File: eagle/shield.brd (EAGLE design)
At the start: 63.2 x 55.9 mm, 12 parts

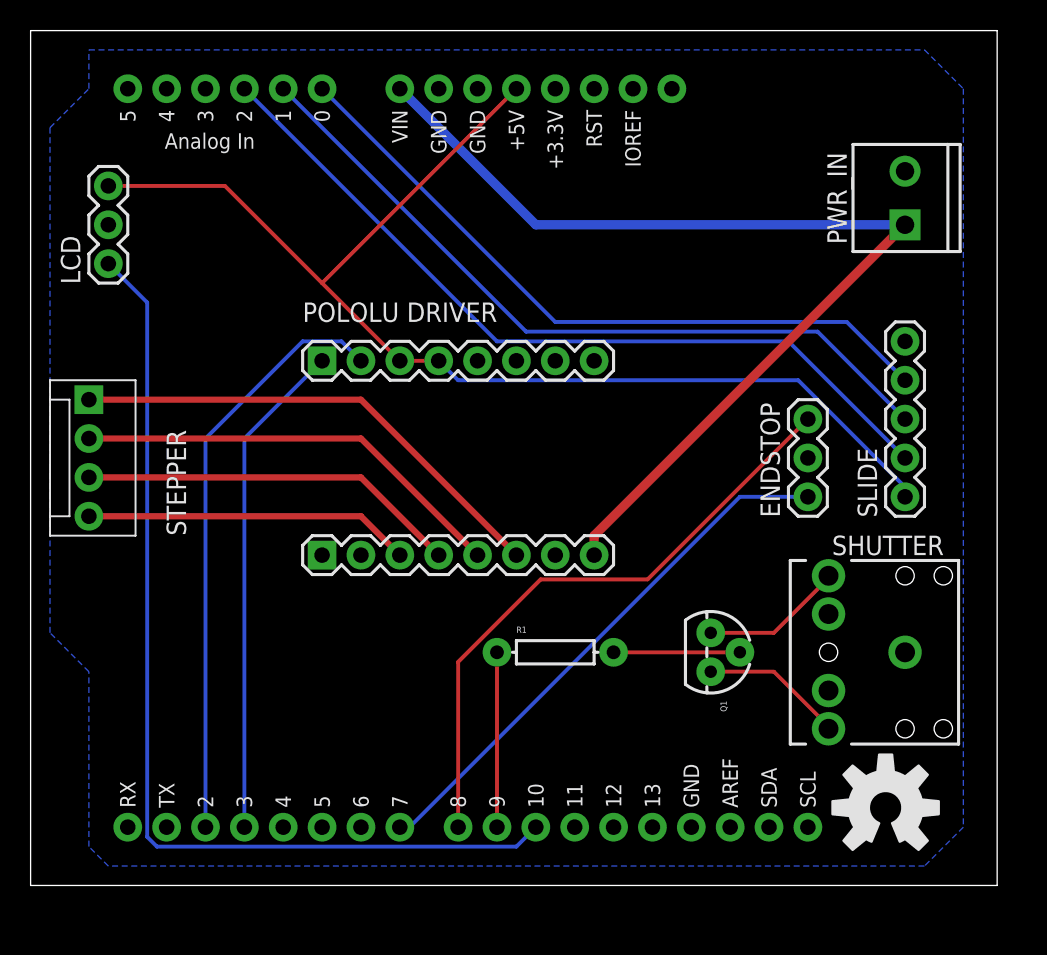
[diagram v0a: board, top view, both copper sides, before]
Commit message: updated shield schematics to include a second joystick and two servos to control pan and tilt
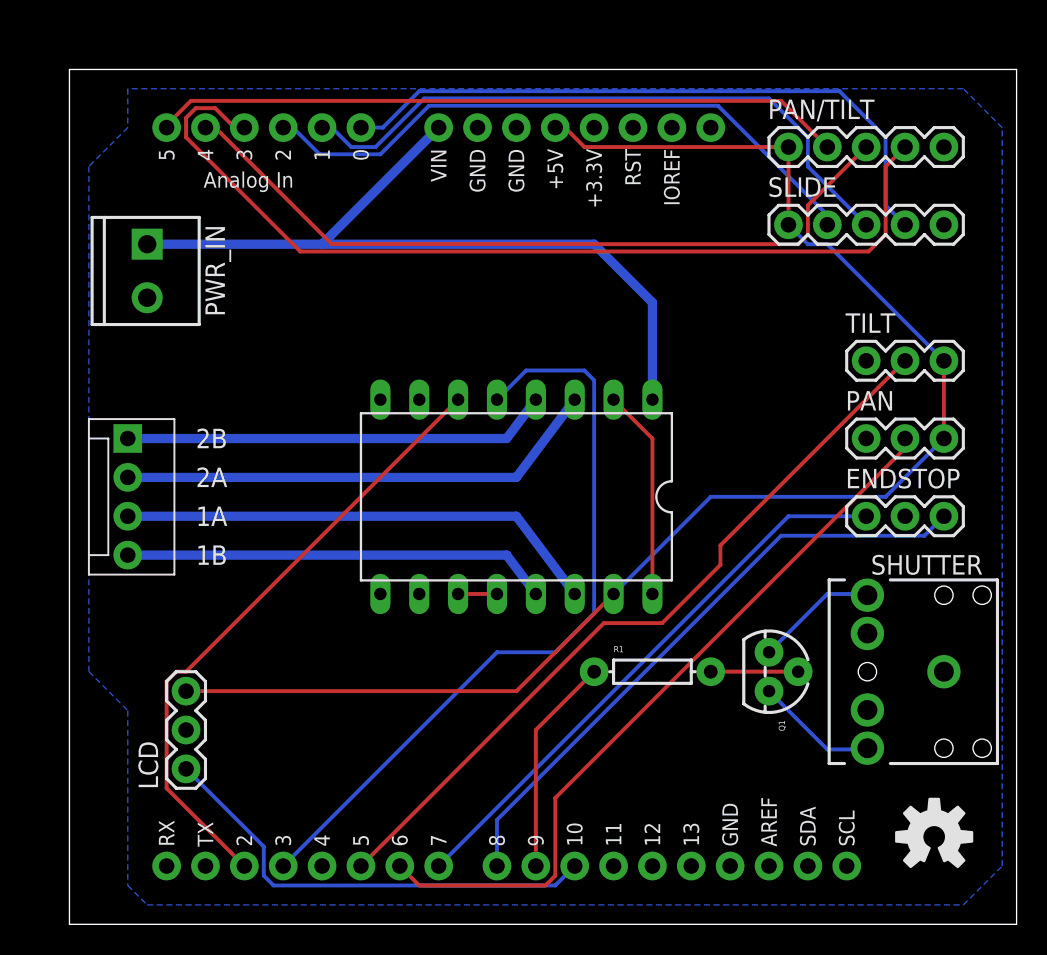
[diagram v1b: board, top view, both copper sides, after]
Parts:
- removed POLOLU_L, POLOLU_R: (no value), SparkFun-Connectors:1X08
- added PAN, TILT: (no value), SparkFun-Connectors:1X03
- added PAN/TILT: (no value), SparkFun-Connectors:1X05
- added SOCKET: POLOLU DRIVER, reprap:DIL16
- LOGO1: value OSHW-LOGOL -> OSHW-LOGOM; device SparkFun-Aesthetics:OSHW-LOGO-L -> SparkFun-Aesthetics:OSHW-LOGO-M
- moved PWR_IN 49.5 mm to (6.35, 67.3), turned to 270 degrees
- moved LCD 33.4 mm to (8.89, 33.0)
- moved SLIDE 19.3 mm to (48.3, 68.6), turned to 0 degrees
- moved R1 6.48 mm to (39.4, 39.4)
- moved Q1 4.02 mm to (47.0, 39.4)
- moved ENDSTOP 4.02 mm to (53.3, 49.5), turned to 0 degrees
- moved LOGO1 3.70 mm to (57.8, 28.6)
- moved MCU 3.59 mm to (62.2, 24.1)
- moved MOTOR 3.59 mm to (5.08, 54.6)
- moved SHUTTER 2.84 mm to (58.4, 39.4)
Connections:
- removed net N$4: MOTOR.1, POLOLU_L.6
- removed net N$5: MOTOR.2, POLOLU_L.5
- removed net N$6: MOTOR.3, POLOLU_L.4
- removed net N$7: MOTOR.4, POLOLU_L.3
- new net 1A: MOTOR.4, SOCKET.5
- new net 1B: MOTOR.3, SOCKET.6
- new net 2A: MOTOR.1, SOCKET.4
- new net 2B: MOTOR.2, SOCKET.3
- new net N$15: MCU.D6, PAN.2
- new net N$18: MCU.D5, TILT.2
- new net N$19: SOCKET.2, SOCKET.8
- new net N$20: MCU.A3, PAN/TILT.4
- new net N$21: MCU.A4, PAN/TILT.3
- new net N$22: MCU.A5, PAN/TILT.2
- new net N$23: SOCKET.11, SOCKET.12
- net GND: now also PAN.1, PAN/TILT.5, TILT.1; no longer POLOLU_L.1, POLOLU_L.7
- net N$1: now also SOCKET.10; no longer POLOLU_R.2
- net N$2: now also SOCKET.9; no longer POLOLU_R.1
- net PWR: now also SOCKET.1; no longer POLOLU_L.8
- net VCC: now also PAN.3, PAN/TILT.1, SOCKET.7, TILT.3; no longer POLOLU_R.3, POLOLU_R.4
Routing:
- net N$20: track 0.00 -> 61.4 mm
- net N$21: track 0.00 -> 50.1 mm
- net N$18: track 0.00 -> 50.0 mm
- net N$15: track 0.00 -> 49.0 mm
- net N$22: track 0.00 -> 45.2 mm
- net N$3: track 64.7 -> 30.2 mm
- net N$4: track 32.1 -> 0.00 mm
- net 2B: track 0.00 -> 31.7 mm
- net 1B: track 0.00 -> 31.7 mm
- net N$5: track 28.6 -> 0.00 mm
- net 2A: track 0.00 -> 27.9 mm
- net 1A: track 0.00 -> 27.9 mm
- net N$6: track 25.0 -> 0.00 mm
- net N$7: track 21.4 -> 0.00 mm
- net VCC: track 78.8 -> 96.1 mm
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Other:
- board size 63.2 x 55.9 mm -> 61.9 x 55.9 mm
- board text added: "1A"
- board text added: "1B"
- board text added: "2A"
- board text added: "2B"
- board text removed: "POLOLU DRIVER"
- board text removed: "STEPPER"

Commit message: refined board design
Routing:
- net N$1: track 40.8 -> 57.9 mm
- net N$18: track 50.0 -> 50.7 mm
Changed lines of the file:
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@@
 <contactref element="MCU" pad="D2"/>
 <contactref element="SOCKET" pad="10"/>
-<wire x1="8.89" y1="39.37" x2="26.67" y2="57.15" width="0.254" layer="1"/>
-<wire x1="8.255" y1="39.37" x2="8.89" y2="39.37" width="0.254" layer="1"/>
-<wire x1="7.62" y1="38.735" x2="8.255" y2="39.37" width="0.254" layer="1"/>
-<wire x1="7.62" y1="31.75" x2="7.62" y2="38.735" width="0.254" layer="1"/>
+<wire x1="7.62" y1="31.75" x2="7.62" y2="41.91" width="0.254" layer="1"/>
 <wire x1="12.7" y1="26.67" x2="7.62" y2="31.75" width="0.254" layer="1"/>
+<wire x1="7.62" y1="41.91" x2="3.81" y2="45.72" width="0.254" layer="1"/>
+<wire x1="3.81" y1="45.72" x2="3.81" y2="55.88" width="0.254" layer="1"/>
+<wire x1="3.81" y1="55.88" x2="6.985" y2="59.055" width="0.254" layer="1"/>
+<wire x1="6.985" y1="59.055" x2="24.765" y2="59.055" width="0.254" layer="1"/>
+<wire x1="24.765" y1="59.055" x2="26.67" y2="57.15" width="0.254" layer="1"/>
 </signal>
 <signal name="N$2">
@@
 <contactref element="PAN" pad="2"/>
 <wire x1="24.13" y1="25.4" x2="22.86" y2="26.67" width="0.254" layer="1"/>
-<wire x1="55.88" y1="53.975" x2="33.02" y2="31.115" width="0.254" layer="1"/>
-<wire x1="55.88" y1="54.61" x2="55.88" y2="53.975" width="0.254" layer="1"/>
 <wire x1="32.385" y1="25.4" x2="24.13" y2="25.4" width="0.254" layer="1"/>
 <wire x1="33.02" y1="26.035" x2="32.385" y2="25.4" width="0.254" layer="1"/>
-<wire x1="33.02" y1="31.115" x2="33.02" y2="26.035" width="0.254" layer="1"/>
+<wire x1="33.02" y1="31.75" x2="33.02" y2="26.035" width="0.254" layer="1"/>
+<wire x1="55.88" y1="54.61" x2="33.02" y2="31.75" width="0.254" layer="1"/>
 </signal>
 <signal name="N$18">
 <contactref element="MCU" pad="D5"/>
 <contactref element="TILT" pad="2"/>
-<wire x1="36.195" y1="42.545" x2="20.32" y2="26.67" width="0.254" layer="1"/>
-<wire x1="55.88" y1="59.69" x2="43.815" y2="47.625" width="0.254" layer="1"/>
-<wire x1="43.815" y1="46.355" x2="43.815" y2="47.625" width="0.254" layer="1"/>
-<wire x1="40.005" y1="42.545" x2="43.815" y2="46.355" width="0.254" layer="1"/>
-<wire x1="36.195" y1="42.545" x2="40.005" y2="42.545" width="0.254" layer="1"/>
+<wire x1="20.32" y1="26.67" x2="20.955" y2="26.67" width="0.254" layer="1"/>
+<wire x1="20.955" y1="26.67" x2="36.195" y2="41.91" width="0.254" layer="1"/>
+<wire x1="36.195" y1="41.91" x2="40.64" y2="41.91" width="0.254" layer="1"/>
+<wire x1="40.64" y1="41.91" x2="48.26" y2="49.53" width="0.254" layer="1"/>
+<wire x1="48.26" y1="49.53" x2="48.26" y2="52.07" width="0.254" layer="1"/>
+<wire x1="48.26" y1="52.07" x2="55.88" y2="59.69" width="0.254" layer="1"/>
 </signal>
 <signal name="N$20">
